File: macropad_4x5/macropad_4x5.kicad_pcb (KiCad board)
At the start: 2 copper layers, 76.2 x 96 mm, 44 parts

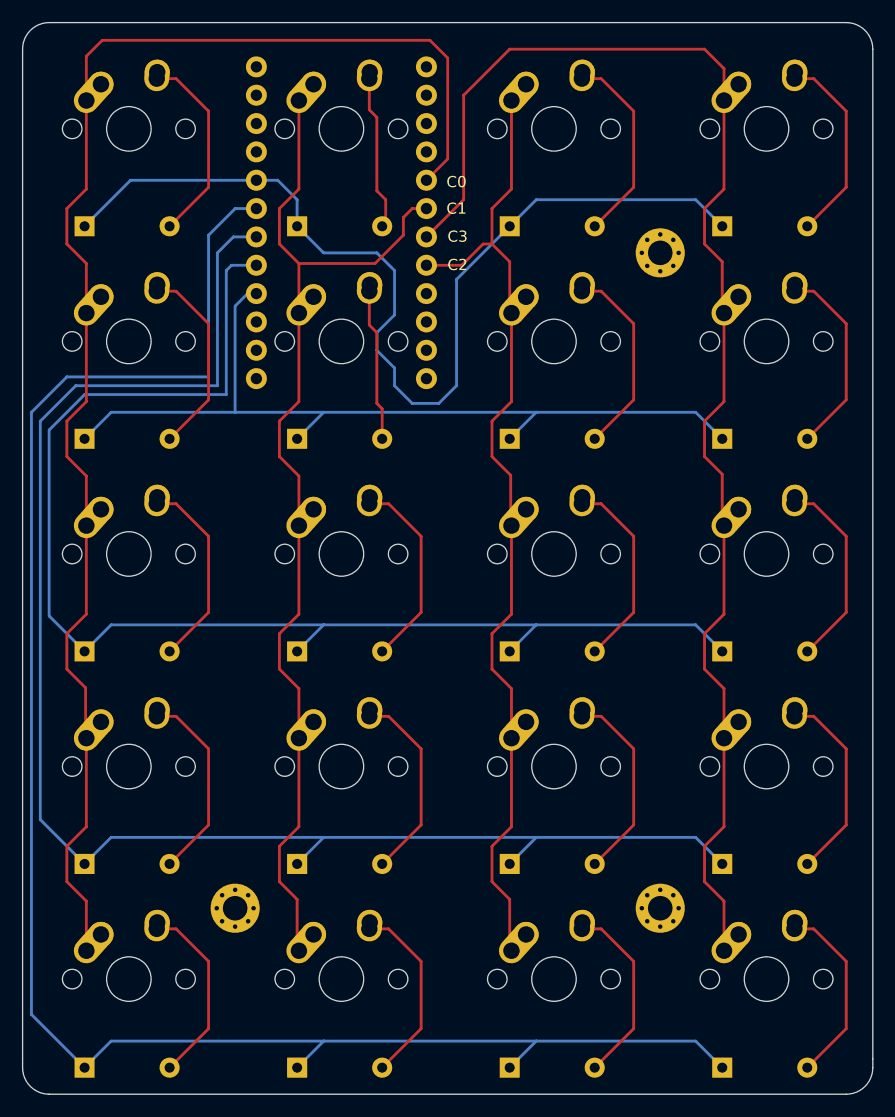
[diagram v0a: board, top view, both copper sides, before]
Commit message: Minor updates to 4x5 macropad files
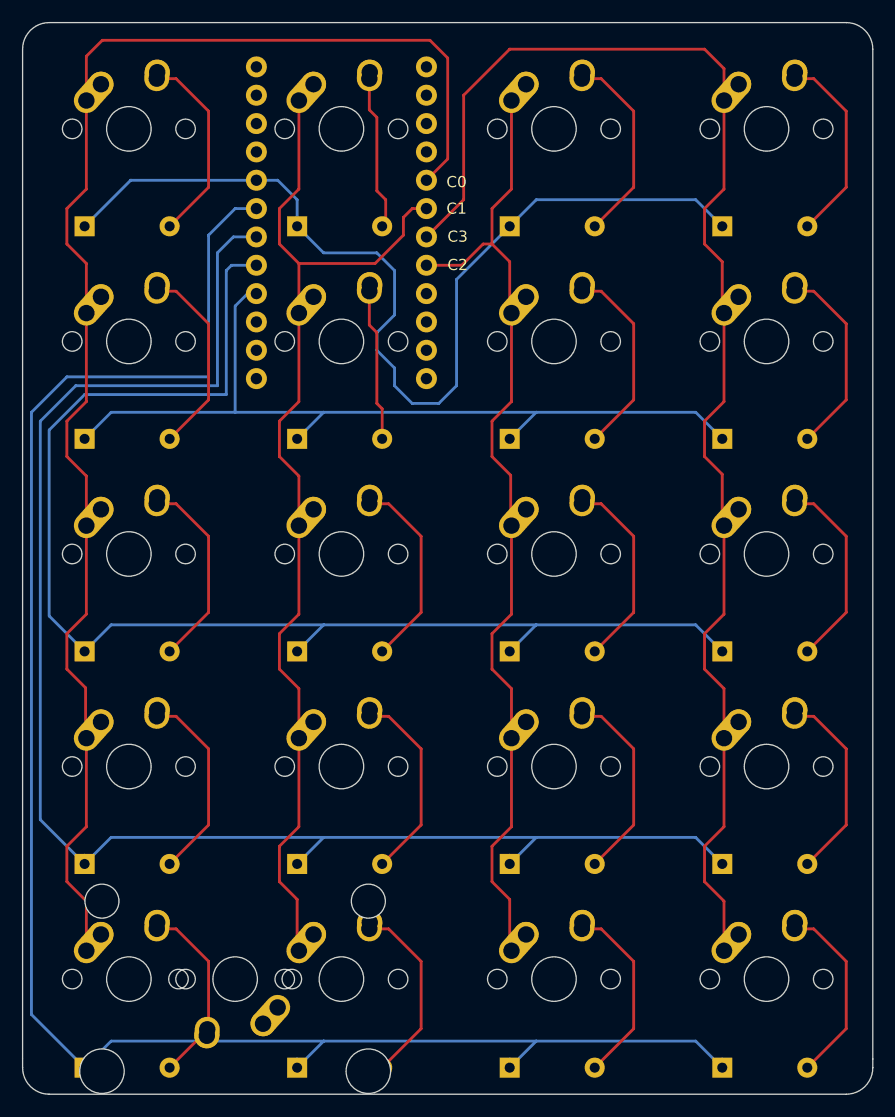
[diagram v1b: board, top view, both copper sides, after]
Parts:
- removed REF** (x3): MountingHole_2.2mm_M2_Pad_Via, MountingHole:MountingHole_2.2mm_M2_Pad_Via
- added MX21: MX-NoLED, MX_Alps_Hybrid:MX-2U-ReversedStabilizers-NoLED, F.Cu at (57.1, 108.0)
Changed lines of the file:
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@@
     (tracks 295)
     (zones 0)
-    (modules 44)
+    (modules 42)
     (nets 45)
   )
@@
     (add_net row4)
   )
-  (module MountingHole:MountingHole_2.2mm_M2_Pad_Via (layer F.Cu)
-    (at 57.15 101.6)
-    (descr "Mounting Hole 2.2mm, M2")
-    (tags "mounting hole 2.2mm m2")
-    (attr virtual)
-    (fp_text reference REF** (at 0 -3.2) (layer F.SilkS) hide
+  (module MX_Alps_Hybrid:MX-2U-ReversedStabilizers-NoLED (layer F.Cu)
+    (at 57.15 107.95 180)
+    (fp_text reference MX21 (at 0 3.175) (layer Dwgs.User)
       (effects (font (size 1 1) (thickness 0.15)))
     )
-    (fp_text value MountingHole_2.2mm_M2_Pad_Via (at 0 3.2) (layer F.Fab)
+    (fp_text value MX-NoLED (at 0 -7.9375) (layer Dwgs.User)
       (effects (font (size 1 1) (thickness 0.15)))
     )
-    (fp_circle (center 0 0) (end 2.45 0) (layer F.CrtYd) (width 0.05))
-    (fp_circle (center 0 0) (end 2.2 0) (layer Cmts.User) (width 0.15))
-    (fp_text user %R (at 0.3 0) (layer F.Fab)
-      (effects (font (size 1 1) (thickness 0.15)))
-    )
-    (pad 1 thru_hole circle (at 1.166726 -1.166726) (size 0.7 0.7) (drill 0.4) (layers *.Cu *.Mask))
-    (pad 1 thru_hole circle (at 0 -1.65) (size 0.7 0.7) (drill 0.4) (layers *.Cu *.Mask))
-    (pad 1 thru_hole circle (at -1.166726 -1.166726) (size 0.7 0.7) (drill 0.4) (layers *.Cu *.Mask))
-    (pad 1 thru_hole circle (at -1.65 0) (size 0.7 0.7) (drill 0.4) (layers *.Cu *.Mask))
-    (pad 1 thru_hole circle (at -1.166726 1.166726) (size 0.7 0.7) (drill 0.4) (layers *.Cu *.Mask))
-    (pad 1 thru_hole circle (at 0 1.65) (size 0.7 0.7) (drill 0.4) (layers *.Cu *.Mask))
-    (pad 1 thru_hole circle (at 1.166726 1.166726) (size 0.7 0.7) (drill 0.4) (layers *.Cu *.Mask))
-    (pad 1 thru_hole circle (at 1.65 0) (size 0.7 0.7) (drill 0.4) (layers *.Cu *.Mask))
-    (pad 1 thru_hole circle (at 0 0) (size 4.4 4.4) (drill 2.2) (layers *.Cu *.Mask))
-  )
-  (module MountingHole:MountingHole_2.2mm_M2_Pad_Via (layer F.Cu)
-    (at 95.25 101.6)
-    (descr "Mounting Hole 2.2mm, M2")
-    (tags "mounting hole 2.2mm m2")
-    (attr virtual)
-    (fp_text reference REF** (at 0 -3.2) (layer F.SilkS) hide
-      (effects (font (size 1 1) (thickness 0.15)))
-    )
-    (fp_text value MountingHole_2.2mm_M2_Pad_Via (at 0 3.2) (layer F.Fab)
-      (effects (font (size 1 1) (thickness 0.15)))
-    )
-    (fp_circle (center 0 0) (end 2.2 0) (layer Cmts.User) (width 0.15))
-    (fp_circle (center 0 0) (end 2.45 0) (layer F.CrtYd) (width 0.05))
-    (fp_text user %R (at 0.3 0) (layer F.Fab)
-      (effects (font (size 1 1) (thickness 0.15)))
-    )
-    (pad 1 thru_hole circle (at 0 0) (size 4.4 4.4) (drill 2.2) (layers *.Cu *.Mask))
-    (pad 1 thru_hole circle (at 1.65 0) (size 0.7 0.7) (drill 0.4) (layers *.Cu *.Mask))
-    (pad 1 thru_hole circle (at 1.166726 1.166726) (size 0.7 0.7) (drill 0.4) (layers *.Cu *.Mask))
-    (pad 1 thru_hole circle (at 0 1.65) (size 0.7 0.7) (drill 0.4) (layers *.Cu *.Mask))
-    (pad 1 thru_hole circle (at -1.166726 1.166726) (size 0.7 0.7) (drill 0.4) (layers *.Cu *.Mask))
-    (pad 1 thru_hole circle (at -1.65 0) (size 0.7 0.7) (drill 0.4) (layers *.Cu *.Mask))
-    (pad 1 thru_hole circle (at -1.166726 -1.166726) (size 0.7 0.7) (drill 0.4) (layers *.Cu *.Mask))
-    (pad 1 thru_hole circle (at 0 -1.65) (size 0.7 0.7) (drill 0.4) (layers *.Cu *.Mask))
-    (pad 1 thru_hole circle (at 1.166726 -1.166726) (size 0.7 0.7) (drill 0.4) (layers *.Cu *.Mask))
-  )
-  (module MountingHole:MountingHole_2.2mm_M2_Pad_Via (layer F.Cu)
-    (at 95.25 42.8625)
-    (descr "Mounting Hole 2.2mm, M2")
-    (tags "mounting hole 2.2mm m2")
-    (attr virtual)
-    (fp_text reference REF** (at 0 -3.2) (layer F.SilkS) hide
-      (effects (font (size 1 1) (thickness 0.15)))
-    )
-    (fp_text value MountingHole_2.2mm_M2_Pad_Via (at 0 3.2) (layer F.Fab)
-      (effects (font (size 1 1) (thickness 0.15)))
-    )
-    (fp_circle (center 0 0) (end 2.45 0) (layer F.CrtYd) (width 0.05))
-    (fp_circle (center 0 0) (end 2.2 0) (layer Cmts.User) (width 0.15))
-    (fp_text user %R (at 0.3 0) (layer F.Fab)
-      (effects (font (size 1 1) (thickness 0.15)))
-    )
-    (pad 1 thru_hole circle (at 1.166726 -1.166726) (size 0.7 0.7) (drill 0.4) (layers *.Cu *.Mask))
-    (pad 1 thru_hole circle (at 0 -1.65) (size 0.7 0.7) (drill 0.4) (layers *.Cu *.Mask))
-    (pad 1 thru_hole circle (at -1.166726 -1.166726) (size 0.7 0.7) (drill 0.4) (layers *.Cu *.Mask))
-    (pad 1 thru_hole circle (at -1.65 0) (size 0.7 0.7) (drill 0.4) (layers *.Cu *.Mask))
-    (pad 1 thru_hole circle (at -1.166726 1.166726) (size 0.7 0.7) (drill 0.4) (layers *.Cu *.Mask))
-    (pad 1 thru_hole circle (at 0 1.65) (size 0.7 0.7) (drill 0.4) (layers *.Cu *.Mask))
-    (pad 1 thru_hole circle (at 1.166726 1.166726) (size 0.7 0.7) (drill 0.4) (layers *.Cu *.Mask))
-    (pad 1 thru_hole circle (at 1.65 0) (size 0.7 0.7) (drill 0.4) (layers *.Cu *.Mask))
-    (pad 1 thru_hole circle (at 0 0) (size 4.4 4.4) (drill 2.2) (layers *.Cu *.Mask))
+    (fp_line (start 5 -7) (end 7 -7) (layer Dwgs.User) (width 0.15))
+    (fp_line (start 7 -7) (end 7 -5) (layer Dwgs.User) (width 0.15))
+    (fp_line (start 5 7) (end 7 7) (layer Dwgs.User) (width 0.15))
+    (fp_line (start 7 7) (end 7 5) (layer Dwgs.User) (width 0.15))
+    (fp_line (start -7 5) (end -7 7) (layer Dwgs.User) (width 0.15))
+    (fp_line (start -7 7) (end -5 7) (layer Dwgs.User) (width 0.15))
+    (fp_line (start -5 -7) (end -7 -7) (layer Dwgs.User) (width 0.15))
+    (fp_line (start -7 -7) (end -7 -5) (layer Dwgs.User) (width 0.15))
+    (fp_line (start -19.05 -9.525) (end 19.05 -9.525) (layer Dwgs.User) (width 0.15))
+    (fp_line (start 19.05 -9.525) (end 19.05 9.525) (layer Dwgs.User) (width 0.15))
+    (fp_line (start -19.05 9.525) (end 19.05 9.525) (layer Dwgs.User) (width 0.15))
+    (fp_line (start -19.05 9.525) (end -19.05 -9.525) (layer Dwgs.User) (width 0.15))
+    (pad "" np_thru_hole circle (at 11.938 -8.255 180) (size 3.9878 3.9878) (drill 3.9878) (layers *.Cu *.Mask))
+    (pad "" np_thru_hole circle (at -11.938 -8.255 180) (size 3.9878 3.9878) (drill 3.9878) (layers *.Cu *.Mask))
+    (pad "" np_thru_hole circle (at 11.938 6.985 180) (size 3.048 3.048) (drill 3.048) (layers *.Cu *.Mask))
+    (pad "" np_thru_hole circle (at -11.938 6.985 180) (size 3.048 3.048) (drill 3.048) (layers *.Cu *.Mask))
+    (pad "" np_thru_hole circle (at 5.08 0 228.0996) (size 1.75 1.75) (drill 1.75) (layers *.Cu *.Mask))
+    (pad "" np_thru_hole circle (at -5.08 0 228.0996) (size 1.75 1.75) (drill 1.75) (layers *.Cu *.Mask))
+    (pad 1 thru_hole circle (at -2.5 -4 180) (size 2.25 2.25) (drill 1.47) (layers *.Cu B.Mask)
+      (net 7 col0))
+    (pad "" np_thru_hole circle (at 0 0 180) (size 3.9878 3.9878) (drill 3.9878) (layers *.Cu *.Mask))
+    (pad 1 thru_hole oval (at -3.81 -2.54 228.0996) (size 4.211556 2.25) (drill 1.47 (offset 0.980778 0)) (layers *.Cu B.Mask)
+      (net 7 col0))
+    (pad 2 thru_hole circle (at 2.54 -5.08 180) (size 2.25 2.25) (drill 1.47) (layers *.Cu B.Mask)
+      (net 14 row4))
+    (pad 2 thru_hole oval (at 2.5 -4.5 266.0548) (size 2.831378 2.25) (drill 1.47 (offset 0.290689 0)) (layers *.Cu B.Mask)
+      (net 14 row4))
   )
   (module MX_Alps_Hybrid:MX-1U-NoLED (layer F.Cu)
